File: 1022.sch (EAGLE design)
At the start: 11 parts, among them J2 HR911105A, J3 USB-MICROB, U1 HLK-RM04, U2 I2C-24C64

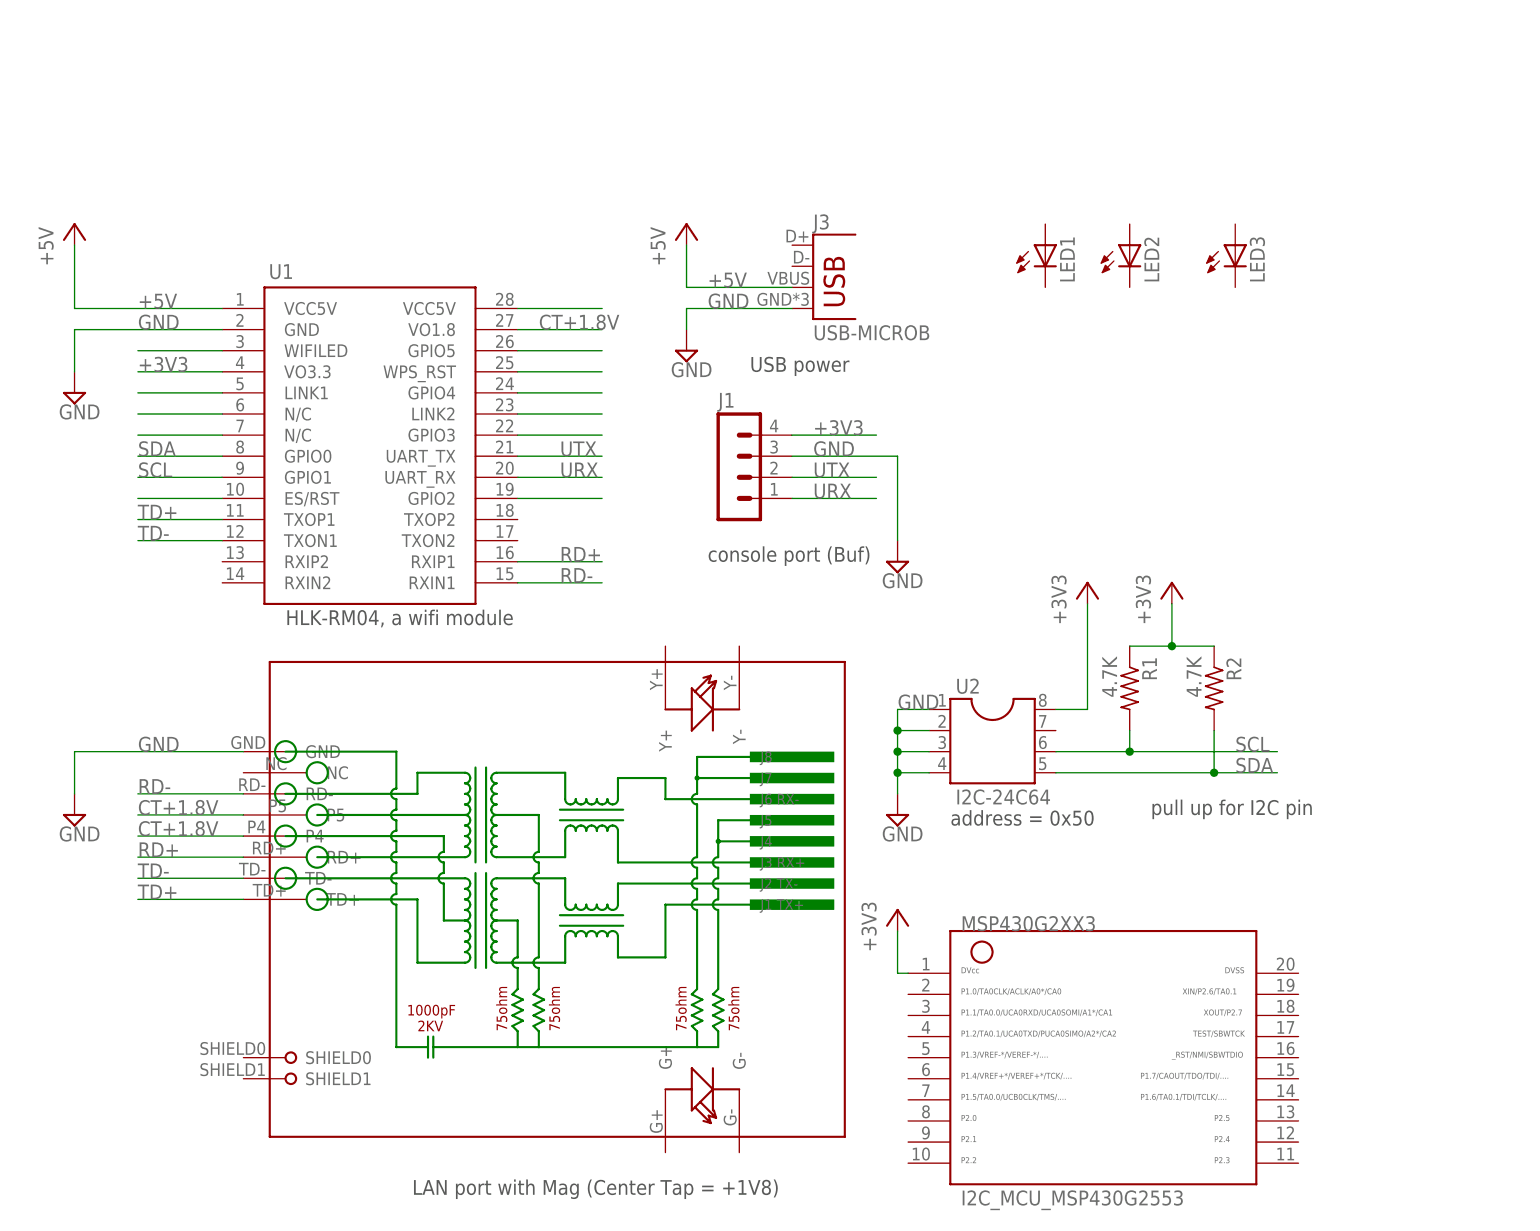
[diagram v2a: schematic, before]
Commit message: add TSSOP package
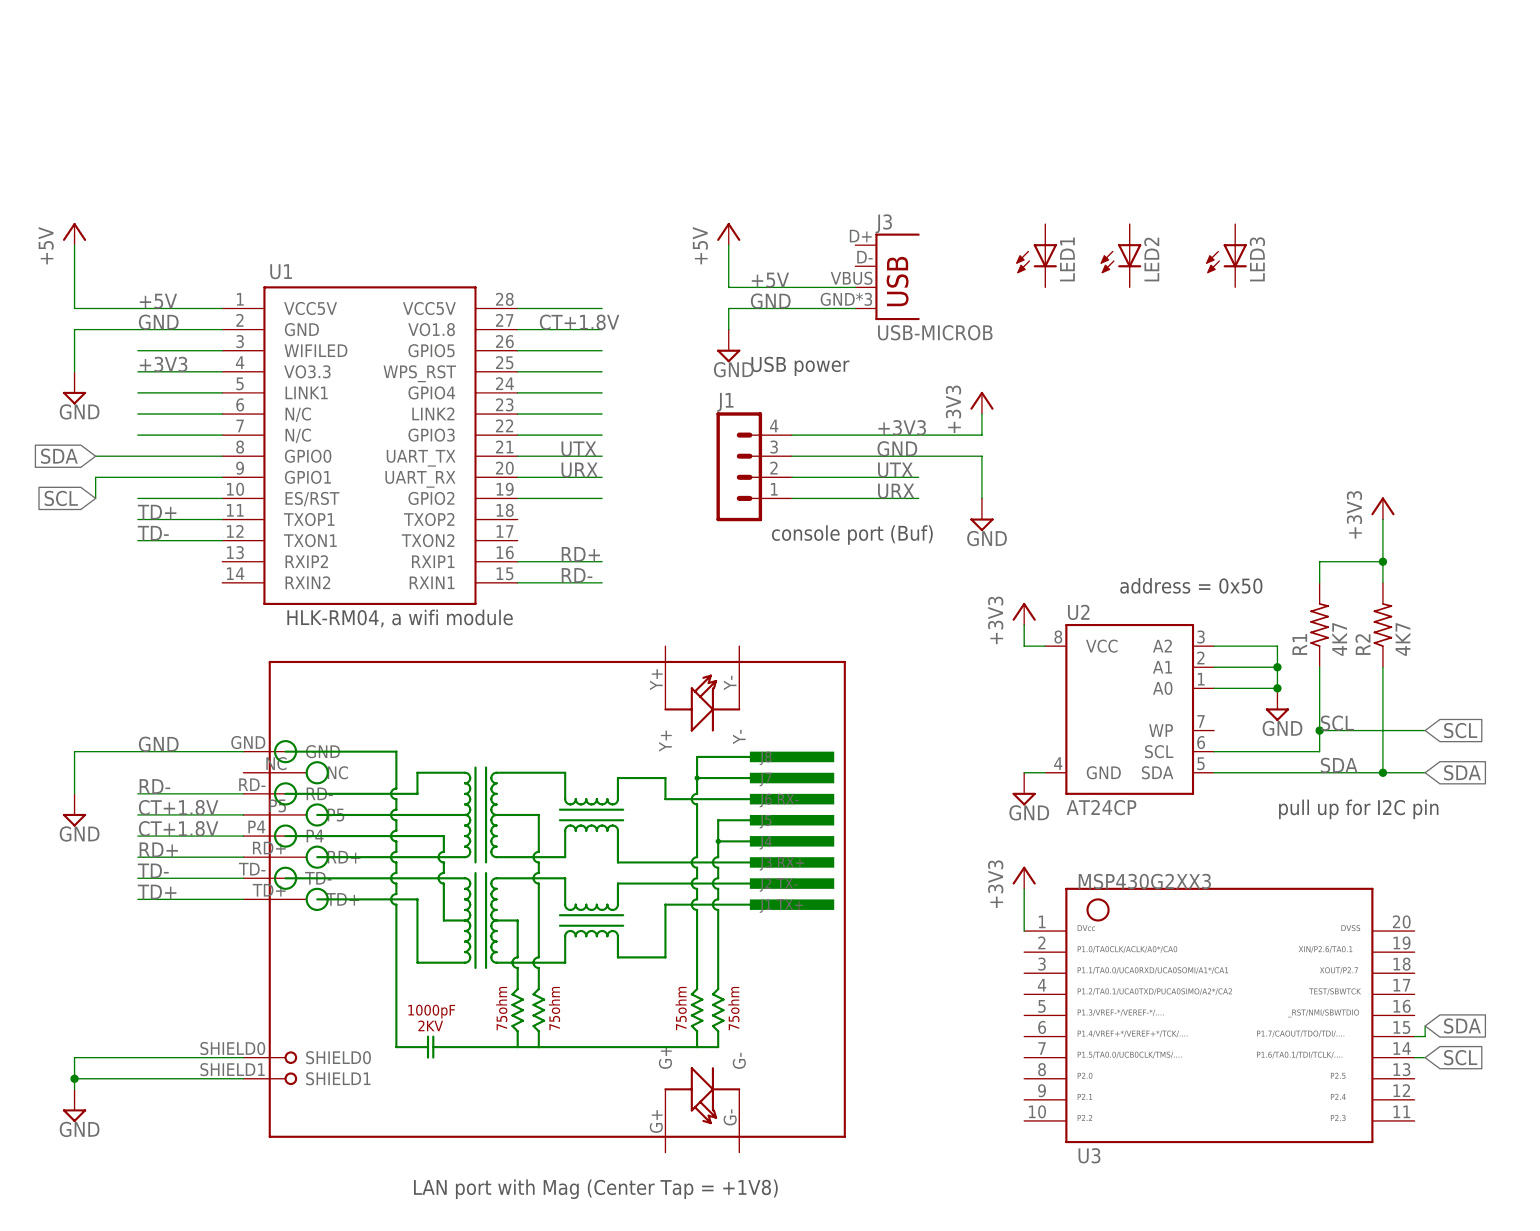
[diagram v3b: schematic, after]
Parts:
- removed I2C_MCU_MSP430G2553: G2XX3---N20, TI_MSP430_v16:G2XX3---N20
- added U3: G2XX3---PW20, TI_MSP430_v16:G2XX3---PW20
- R1, R2: value 4.7K -> 4K7; device rcl:R-US_0207/10 -> rcl:R-US_M0805
- U2: value I2C-24C64 -> AT24CP; device ic-package:DIL8S -> atmel:AT24CP
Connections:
- net +3V3: now also R1.2, R2.2, U2.VCC, U3.1; no longer I2C_MCU_MSP430G2553.1, R1.1, R2.1, U2.8
- net GND: now also J2.SHIELD0, J2.SHIELD1, U2.A0, U2.A1, U2.A2, U2.GND; no longer U2.1, U2.2, U2.3, U2.4
- net SCL: now also R1.1, U2.SCL, U3.14; no longer R1.2, U2.6
- net SDA: now also R2.1, U2.SDA, U3.15; no longer R2.2, U2.5
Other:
- moved on the sheet: J3, R1, R2

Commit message: add placement
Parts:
- added C1, C2: 0.1uF, rcl:C-EUC0603
- R1, R2: device rcl:R-US_M0805 -> rcl:R-US_R0603
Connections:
- net +3V3: now also C1.1, C2.1
- net GND: now also C1.2, C2.2
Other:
- moved on the sheet: J1, J3, LED1, LED2, LED3, R2
